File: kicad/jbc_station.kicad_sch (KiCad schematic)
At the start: 16 parts

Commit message: Design input/output power stage
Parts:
- removed D?: LED, symbol Device:LED
- removed R?: 100, symbol Device:R
- removed R? (x4): 2k7, symbol Device:R
- removed U?: LPH8836, symbol custom_symbols:LPH8836
- removed U?: INA226, Package_SO:VSSOP-10_3x3mm_P0.5mm, symbol Analog_ADC:INA226
- added C62: 100n, Capacitor_SMD:C_0805_2012Metric, symbol Device:C
- added C63: 2.2u, Capacitor_SMD:C_0805_2012Metric, symbol Device:C
- added L4: 1u, symbol Device:L
- added R1: 0R_0603, 4ms_Resistor:R_0603, symbol PCM_4ms_Resistor:0R_0603
- added U8: INA3221, Package_DFN_QFN:Texas_RGV_S-PVQFN-N16_EP2.1x2.1mm, symbol Power_Management:INA3221
- C1: renamed from C?; value C -> 47n; footprint (none) -> Capacitor_SMD:C_0805_2012Metric
- C2: renamed from C?; value C -> 2.2u; footprint (none) -> Capacitor_SMD:C_0805_2012Metric
- C3, C4, C5, C6, C7: renamed from C?; value C -> 100n; footprint (none) -> Capacitor_SMD:C_0805_2012Metric
- gave numbers to parts that had none: 1
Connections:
- net +3.3V: now also L4.2; no longer U1.9 (VREF+)
- net GND: now also C62.1, C63.1, R1.2
- net at U1.22 (VCAP1): now also C62.2; no longer C7.2
- new net +3.3VA: C63.2, C7.2, L4.1, U1.9 (VREF+)
- new net GNDPWR: R1.1
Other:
- added sheet int-out1 (in-out.kicad_sch)
- added sheet int-out2 (in-out.kicad_sch)
- added sheet int-out3 (in-out.kicad_sch)
- moved on the sheet: C1, C2, C3, C4, C5, C6, C7

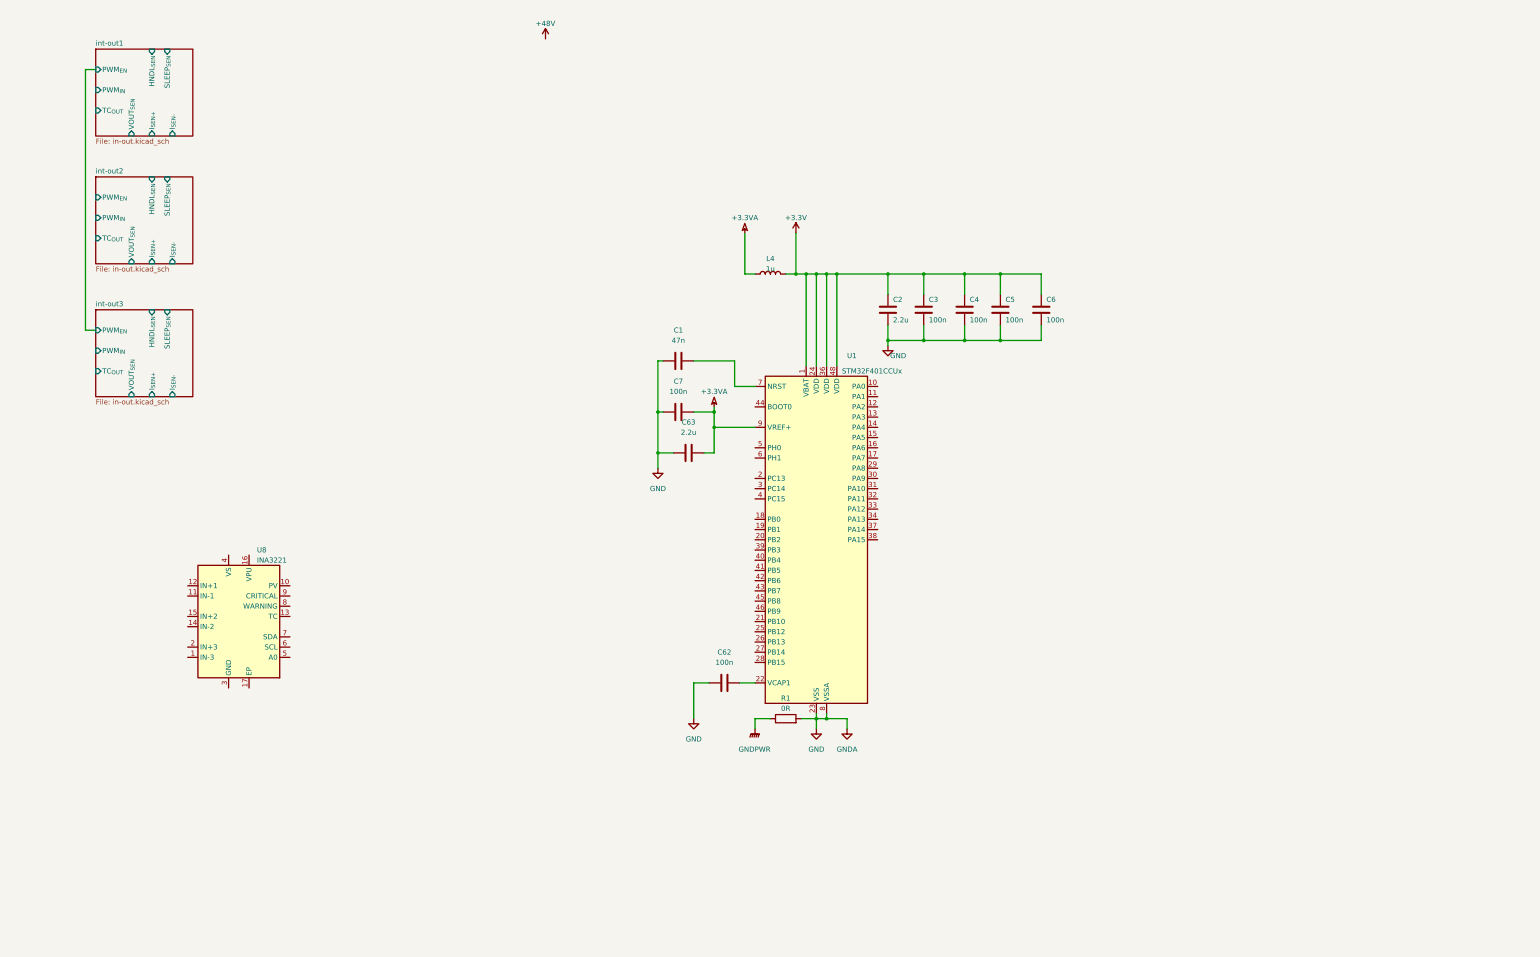
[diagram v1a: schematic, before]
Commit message: Add regulators
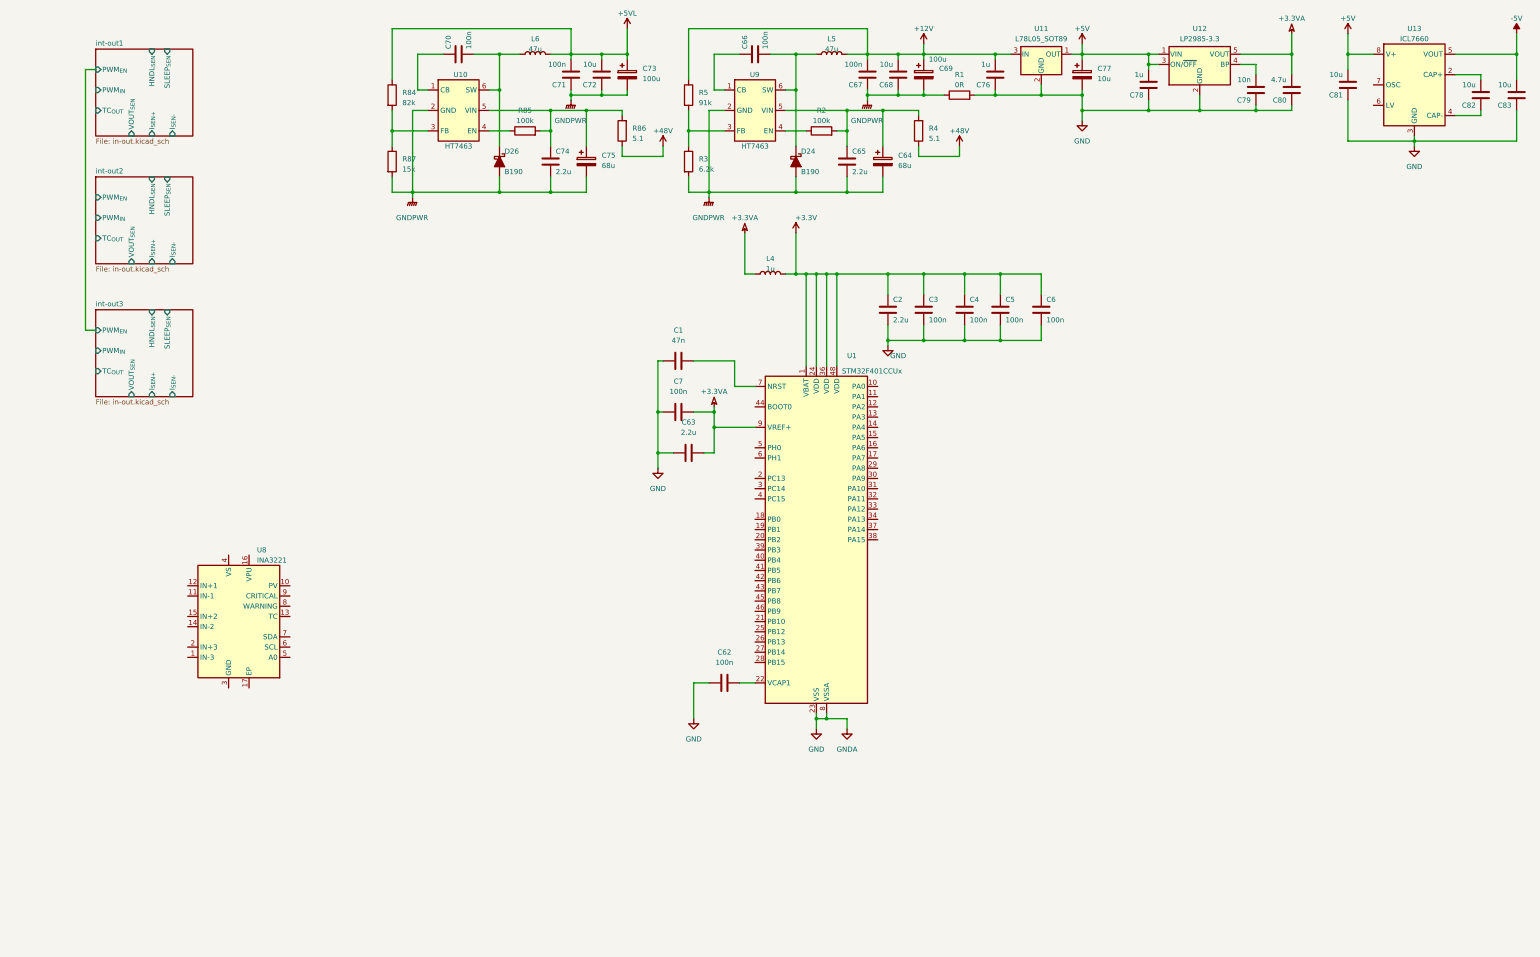
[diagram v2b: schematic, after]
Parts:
- added C64, C75: 68u, symbol Device:C_Polarized
- added C65, C74: 2.2u, Capacitor_SMD:C_0805_2012Metric, symbol Device:C
- added C66, C67, C70, C71: 100n, Capacitor_SMD:C_0805_2012Metric, symbol Device:C
- added C68, C72, C81, C82, C83: 10u, Capacitor_SMD:C_0805_2012Metric, symbol Device:C
- added C69, C73: 100u, symbol Device:C_Polarized
- added C76, C78: 1u, Capacitor_SMD:C_0805_2012Metric, symbol Device:C
- added C77: 10u, symbol Device:C_Polarized
- added C79: 10n, Capacitor_SMD:C_0805_2012Metric, symbol Device:C
- added C80: 4.7u, Capacitor_SMD:C_0805_2012Metric, symbol Device:C
- added D24, D26: B190, Diode_SMD_AKL:D_SMA, symbol PCM_Diode_Schottky_AKL:B190
- added L5, L6: 47u, symbol Device:L
- added R2, R85: 100k, symbol Device:R
- added R3: 6.2k, symbol Device:R
- added R4, R86: 5.1, symbol Device:R
- added R5: 91k, symbol Device:R
- added R84: 82k, symbol Device:R
- added R87: 15k, symbol Device:R
- added U10, U9: HT7463, Package_TO_SOT_SMD:SOT-23-6_Handsoldering, symbol custom_symbols:HT7463
- added U11: L78L05_SOT89, Package_TO_SOT_SMD:SOT-89-3, symbol Regulator_Linear:L78L05_SOT89
- added U12: LP2985-3.3, Package_TO_SOT_SMD:SOT-23-5, symbol Regulator_Linear:LP2985-3.3
- added U13: ICL7660, symbol Regulator_SwitchedCapacitor:ICL7660
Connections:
- net +3.3VA: now also C80.2, U12.5 (VOUT)
- net +48V: now also R4.1, R86.1
- net GND: now also C76.1, C77.2, C78.1, C79.1, C80.1, C81.1, C83.1, U11.2 (GND), U12.2 (GND), U13.3 (GND)
- net GNDPWR: now also C64.2, C65.2, C67.1, C68.1, C69.2, C71.1, C72.1, C73.2, C74.2, C75.2, D24.2 (A), D26.2 (A), R3.2, R87.2, U10.2 (GND), U9.2 (GND)
- new net: C66.1, U9.1 (CB)
- new net: C66.2, D24.1 (K), L5.1, U9.6 (SW)
- new net: R2.1, U9.4 (EN)
- new net: C64.1, C65.1, R2.2, R4.2, U9.5 (VIN)
- new net: C79.2, U12.4 (BP)
- new net: C70.1, U10.1 (CB)
- new net: R84.2, R87.1, U10.3 (FB)
- new net: R85.1, U10.4 (EN)
- new net: C74.1, C75.1, R85.2, R86.2, U10.5 (VIN)
- new net: C70.2, D26.1 (K), L6.1, U10.6 (SW)
- new net: R3.1, R5.2, U9.3 (FB)
- new net: C82.2, U13.2 (CAP+)
- new net: C82.1, U13.4 (CAP-)
- new net +12V: C67.2, C68.2, C69.1, C76.2, L5.2, R5.1, U11.3 (IN)
- new net +5V: C77.1, C78.2, C81.2, U11.1 (OUT), U12.1 (VIN), U12.3 (ON/~{OFF}), U13.8 (V+)
- new net +5VL: C71.2, C72.2, C73.1, L6.2, R84.1
- new net -5V: C83.2, U13.5 (VOUT)

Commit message: Add current sensor
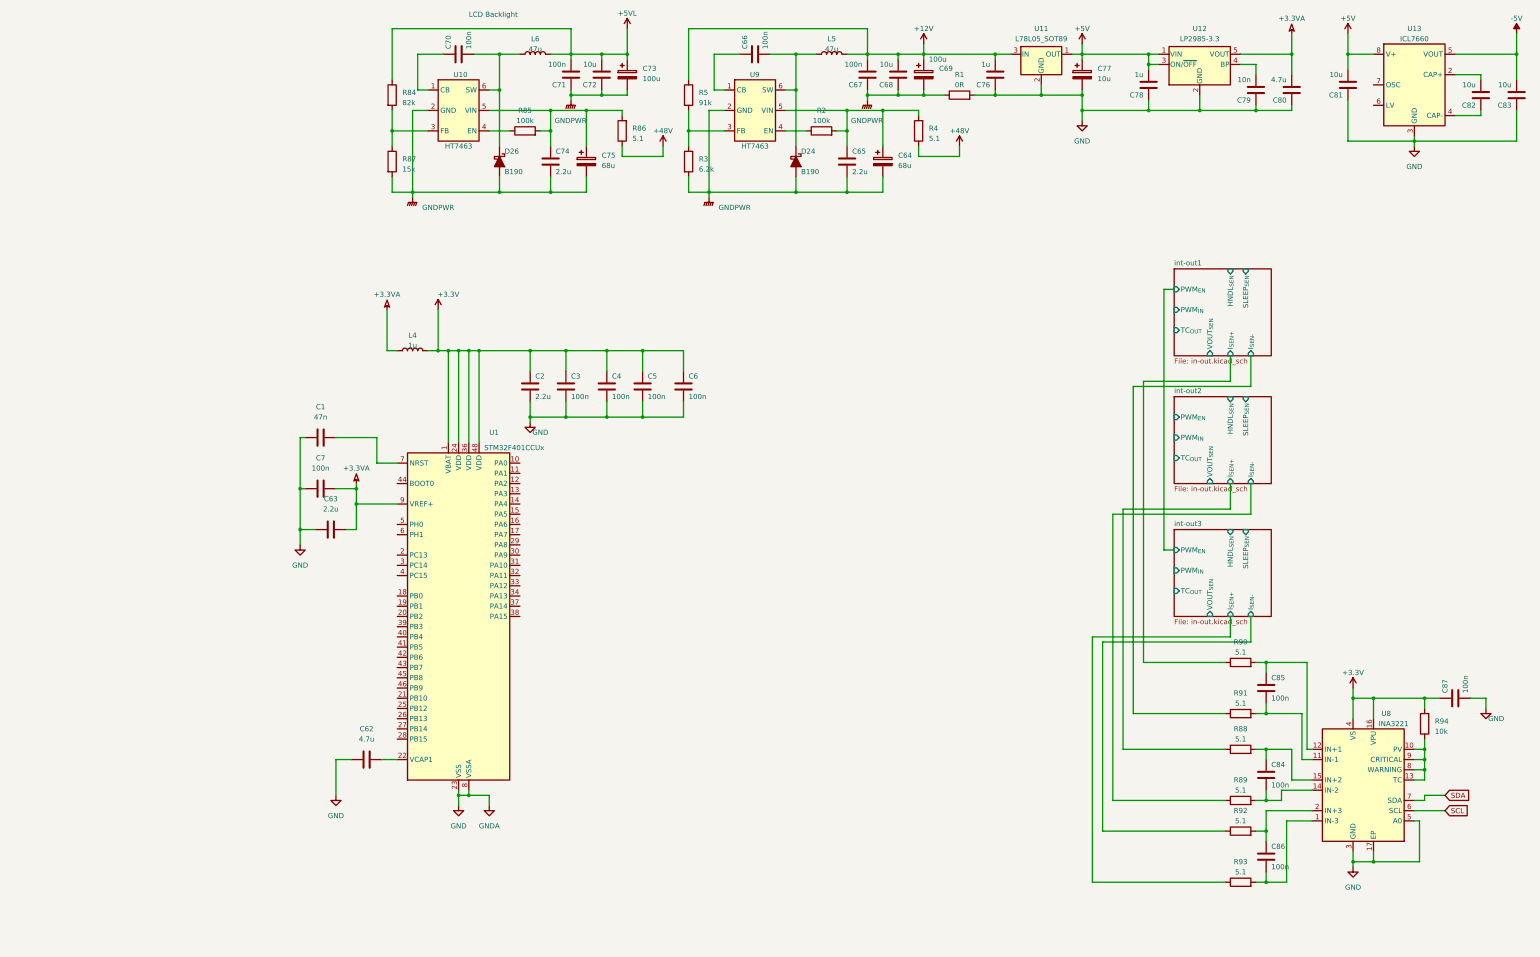
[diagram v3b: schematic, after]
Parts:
- added C84, C85, C86, C87: 100n, Capacitor_SMD:C_0805_2012Metric, symbol Device:C
- added R88, R89, R90, R91, R92, R93: 5.1, symbol Device:R
- added R94: 10k, symbol Device:R
- C62: value 100n -> 4.7u; footprint Capacitor_SMD:C_0805_2012Metric -> Capacitor_SMD:C_1206_3216Metric_Pad1.33x1.80mm_HandSolder
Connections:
- net +3.3V: now also U8.16 (VPU), U8.4 (VS), C87.1, R94.2
- net GND: now also U8.17 (EP), U8.3 (GND), U8.5 (A0), C87.2
- net int-out1/I_{SEN+}: now also R90.1
- net int-out1/I_{SEN-}: now also R91.1
- net int-out2/I_{SEN+}: now also R88.1
- net int-out2/I_{SEN-}: now also R89.1
- net int-out3/I_{SEN+}: now also R93.1
- net int-out3/I_{SEN-}: now also R92.1
- net at U8.1 (IN-3): now also C86.2, R93.2
- net at U8.10 (PV): now also U8.13 (TC), U8.8 (WARNING), U8.9 (CRITICAL), R94.1
- net at U8.11 (IN-1): now also C85.2, R91.2
- net at U8.12 (IN+1): now also C85.1, R90.2
- net at U8.14 (IN-2): now also C84.2, R89.2
- net at U8.15 (IN+2): now also C84.1, R88.2
- net at U8.2 (IN+3): now also C86.1, R92.2
- net SCL: now reaches U8.6 (SCL)
- net SDA: now reaches U8.7 (SDA)
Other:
- note added: "LCD Backlight"
- moved on the sheet: C1, C2, C3, C4, C5, C6, C62, C63, C7, L4, U1, U8

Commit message: Most of the main board is done
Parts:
- added C88: 100n, Capacitor_SMD:C_0805_2012Metric, symbol Device:C
- added C89, C90: 22p, Capacitor_SMD:C_0805_2012Metric, symbol Device:C
- added J19: Conn_01x05, symbol Connector_Generic:Conn_01x05
- added R100, R97, R98, R99: 1.8k, symbol Device:R
- added R95, R96: 10k, symbol Device:R
- added U14: M24C64, Package_SO:SOIC-8_3.9x4.9mm_P1.27mm, symbol Memory_EEPROM:M24C02-WMN
- added Y1: Crystal, PCM_Crystal_AKL:Crystal_SMD_MicroCrystal_MS1V-T1K, symbol Device:Crystal
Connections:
- net SCL is gone; now on net SCL_{1}: U8.6 (SCL)
- net SDA is gone; now on net SDA_{1}: U8.7 (SDA)
- net +3.3V: now also C88.2, R100.2, R97.2, R98.2, R99.2, U14.8 (VCC)
- net GND: now also U1.44 (BOOT0), C89.2, C90.2, J19.4 (Pin_4), R95.1, R96.1
- net int-out3/I_{SEN+}: now also R92.1; no longer R93.1
- net int-out3/I_{SEN-}: now also R93.1; no longer R92.1
- net HNDL_{SEN}1: now reaches U1.10 (PA0)
- net TC_{OUT}1: now reaches U1.11 (PA1)
- net V_{OUT}1: now reaches U1.12 (PA2)
- net HNDL_{SEN}2: now reaches U1.13 (PA3)
- net TC_{OUT}2: now reaches U1.14 (PA4)
- net V_{OUT}2: now reaches U1.15 (PA5)
- net HNDL_{SEN}3: now reaches U1.16 (PA6)
- net TC_{OUT}3: now reaches U1.17 (PA7)
- net V_{OUT}3: now reaches U1.18 (PB0)
- net POWER_BREAK: now reaches U1.19 (PB1)
- net DISP_{CS}: now reaches U1.2 (PC13)
- net INT_{KEY}: now reaches U1.20 (PB2)
- net SCL_{2}: now reaches U1.21 (PB10)
- net SCL_{2}: now also R99.1
- net SDA_{2}: now reaches U1.25 (PB12)
- net SDA_{2}: now also R100.1
- net SLEEP_{SEN}1: now reaches U1.26 (PB13)
- net SLEEP_{SEN}2: now reaches U1.27 (PB14)
- net SLEEP_{SEN}3: now reaches U1.28 (PB15)
- net PWM_{IN}1: now reaches U1.29 (PA8)
- net DISP_{RESET}: now reaches U1.3 (PC14)
- net PWM_{IN}2: now reaches U1.30 (PA9)
- net PWM_{IN}3: now reaches U1.31 (PA10)
- net BT_{TX}: now reaches U1.32 (PA11)
- net BT_{RX}: now reaches U1.33 (PA12)
- net SWDIO: now reaches U1.34 (PA13)
- net SWDIO: now also J19.2 (Pin_2)
- net SWCLK: now reaches U1.37 (PA14)
- net SWCLK: now also J19.3 (Pin_3)
- net SWO: now reaches U1.39 (PB3)
- net SWO: now also J19.5 (Pin_5)
- net DISP_{A0}: now reaches U1.4 (PC15)
- net BL_{RED}: now reaches U1.40 (PB4)
- net BL_{RED}: now also R95.2
- net BL_{GREEN}: now reaches U1.41 (PB5)
- net BL_{GREEN}: now also R96.2
- net BARCODE_{TX}: now reaches U1.42 (PB6)
- net BARCODE_{RX}: now reaches U1.43 (PB7)
- net SCL_{1}: now reaches U1.45 (PB8)
- net SCL_{1}: now also R97.1, U14.6 (SCL)
- net SDA_{1}: now reaches U1.46 (PB9)
- net SDA_{1}: now also R98.1, U14.5 (SDA)
- net at U1.5 (PH0): now also C90.1, Y1.1
- net at U1.6 (PH1): now also C89.1, Y1.2
- new net: C88.1, U14.1 (E0), U14.2 (E1), U14.3 (E2), U14.4 (VSS), U14.7 (~{WC})
- new net +3V3: J19.1 (Pin_1)
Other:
- sheet int-out1 ports: added V_{OUT}; removed VOUT_{SEN}
- sheet int-out2 ports: added V_{OUT}; removed VOUT_{SEN}
- sheet int-out3 ports: added V_{OUT}; removed VOUT_{SEN}
- moved on the sheet: C1, C2, C3, C4, C5, C6, C62, C63, C7, C84, C85, C86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
